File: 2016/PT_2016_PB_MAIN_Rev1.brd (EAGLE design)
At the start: 150.9 x 202.8 mm, 121 parts, among them Q1 Q_IRFS7437PbF, Q11 Q_IRFS7437PbF, Q12 2N7002, Q14 Q_IRFS7437PbF, Q16 Q_IRFS7437PbF, Q20 Q_IRFS7437PbF, Q6 Q_IRFS7437PbF, Q7 Q_IRFS7437PbF, Q9 Q_IRFS7437PbF

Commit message: Continued routing, rearranged some things
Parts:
- moved C45 45.9 mm to (125.8, 8.83), turned to 0 degrees
- moved C46 44.0 mm to (116.4, 13.8)
- moved C20 34.0 mm to (139.6, 80.7), flipped to the bottom
- moved 12V-AUX 29.2 mm to (137.9, 43.9)
- moved C43 29.2 mm to (127.3, 42.2)
- moved LED2 29.2 mm to (142.2, 34.0)
- moved R10 29.2 mm to (135.4, 34.0)
- moved U$21 29.2 mm to (128.8, 50.3)
- moved C6 29.2 mm to (127.3, 38.3)
- moved Q12 17.2 mm to (83.1, 70.1)
- moved R15 15.3 mm to (83.4, 65.3), turned to 270 degrees
- moved R8 12.5 mm to (134.6, 13.5)
- moved LED3 12.4 mm to (142.0, 13.5)
- moved 5V-AUX 12.0 mm to (138.2, 23.6)
- moved C19 11.8 mm to (119.6, 40.3), flipped to the bottom
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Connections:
- removed net 5V_AUX: U$3.P$6
- removed net N$21: U$12.DI
- removed net N$33: U$24.DI
- removed net N$43: U$4.PC4
- removed net N$48: U$4.PC5
- removed net N$65: U$4.PH2
- removed net N$91: U$4.PP0
- removed net N$92: U$4.PP1
- removed net N$93: U$4.PP2
- removed net N$97: U$4.+5V_1, U$4.+5V_2
- removed net N$99: U$4.GND_1, U$4.GND_2, U$4.GND_3, U$4.GND_4
- removed net RXD: U$12.RO
- removed net RXD1: U$24.RO
- new net RX1: U$12.RO, U$4.PC4
- new net RX2: U$24.RO, U$4.PP0
- new net TX1: U$12.DI, U$4.PC5
- new net TX2: U$24.DI, U$4.PP1
- net +5V: now also U$4.+5V_1, U$4.+5V_2
- net 12V-IMEAS: now also U$4.PH2
- net 5V-AUX: now also U$3.P$6
- net GND: now also U$4.GND_1, U$4.GND_2, U$4.GND_3, U$4.GND_4
- net PRIMARY-VMEAS: now also U$4.PP2
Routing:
- net +5V: track 228.2 -> 466.6 mm, vias 0 -> 3
- net TX2: track 0.00 -> 116.7 mm, vias 0 -> 1
- net RX2: track 0.00 -> 113.9 mm, vias 0 -> 1
- net 12V-IMEAS: track 0.00 -> 102.3 mm
- net TX1: track 0.00 -> 41.8 mm
- net RX1: track 0.00 -> 39.0 mm
- net PRIMARY-VMEAS: track 3.76 -> 34.7 mm
- net N$7: track 31.7 -> 11.8 mm
- net N$12: track 12.9 -> 0.00 mm
- net 5V-AUX: track 0.00 -> 11.8 mm
- net GND: track 153.0 -> 145.3 mm, vias 29 -> 28
- net N$4: track 56.0 -> 57.0 mm
- net N$34: track 3.70 -> 4.47 mm
- added copper zone on layer 1, net 5V-AUX
- added copper zone on layer 1, net N$7

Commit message: Continued routing.
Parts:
- moved C6 18.3 mm to (127.8, 56.6)
- moved C43 15.7 mm to (133.3, 56.6), turned to 180 degrees
- moved R10 0.76 mm to (134.6, 34.0)
- moved C46 0.60 mm to (116.4, 13.2), turned to 270 degrees
- moved C45 0.35 mm to (125.4, 8.86), turned to 270 degrees
- moved C7 0.25 mm to (16.5, 128.5), turned to 270 degrees
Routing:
- net +5V: track 466.6 -> 586.4 mm, vias 3 -> 4
- net 12V-IMEAS: track 102.3 -> 141.8 mm
- net N$9: track 0.00 -> 14.1 mm, vias 0 -> 1
- net N$12: track 0.00 -> 8.19 mm
- net 5V-AUX: track 11.8 -> 15.0 mm
- net N$15: track 0.00 -> 2.11 mm
- net N$14: track 0.00 -> 1.63 mm, vias 0 -> 1
- net GND: track 145.3 -> 144.1 mm, vias 28 -> 31
- net N$46: track 3.96 -> 4.72 mm
- added copper zone on layer 16, net 5V-AUX
- removed copper zone on layer 1, net 5V-AUX

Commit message: Routesss
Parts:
- removed U$22: TEST, MRDT-2015-General:TEST
- moved D2 14.8 mm to (76.2, 17.7)
- moved C45 7.66 mm to (118.6, 5.27), turned to 0 degrees
- moved BATT-NEG 6.86 mm to (94.5, 8.89)
- moved C46 2.98 mm to (113.5, 13.9), turned to 180 degrees
- renumbered PALPATINE-12V to POE-12V, SIDEOUS-12V to FINN-12V, U$3 to REY-5V
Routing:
- net N$7: track 11.8 -> 55.8 mm
- net PRIMARY-VMEAS: track 34.7 -> 33.4 mm
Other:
- board text added: "-"
- board text added: "REY-5V"

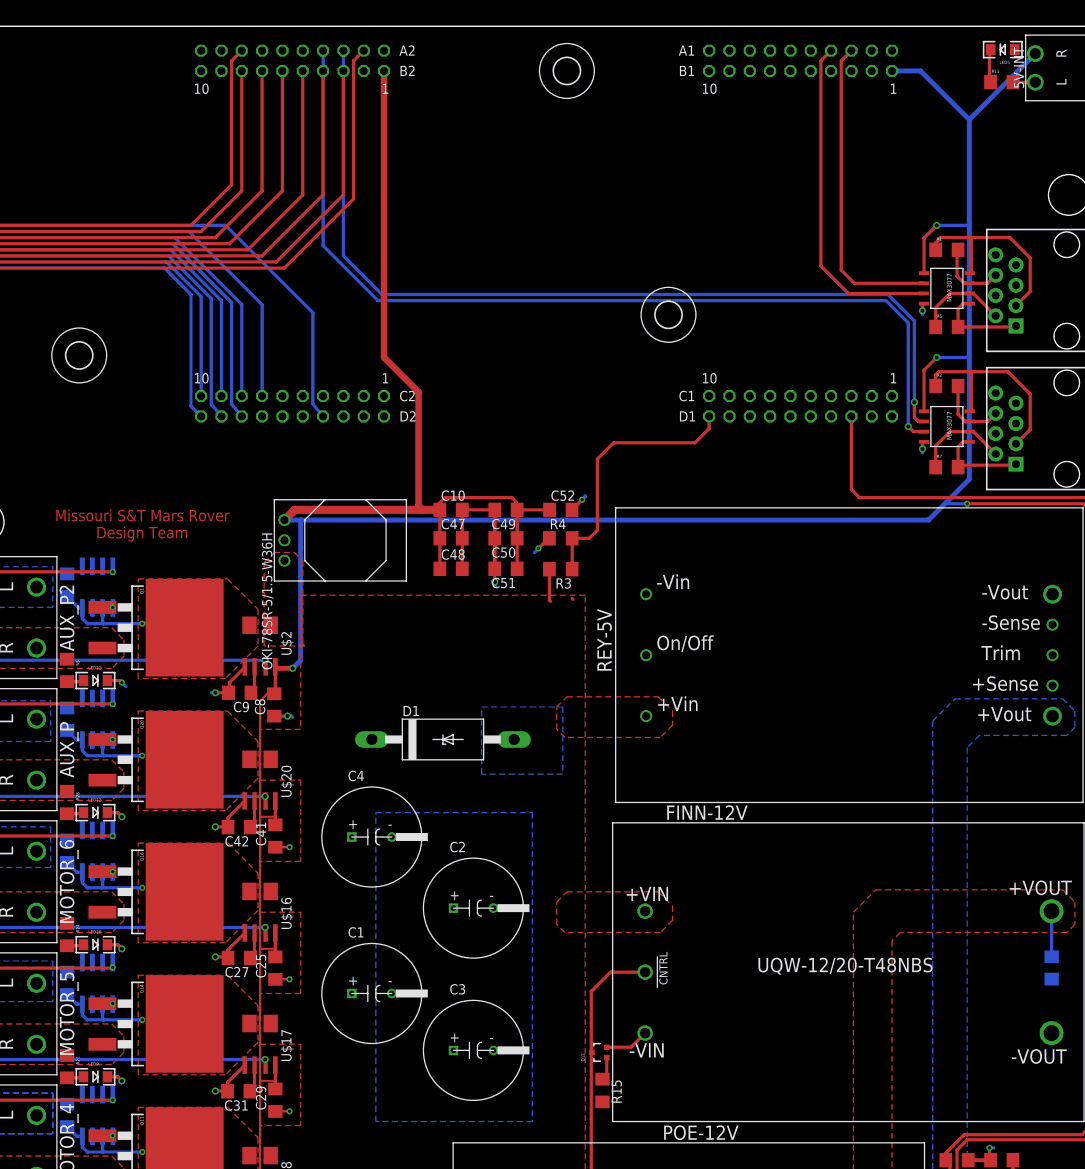
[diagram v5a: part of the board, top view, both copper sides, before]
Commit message: Minor routing changes
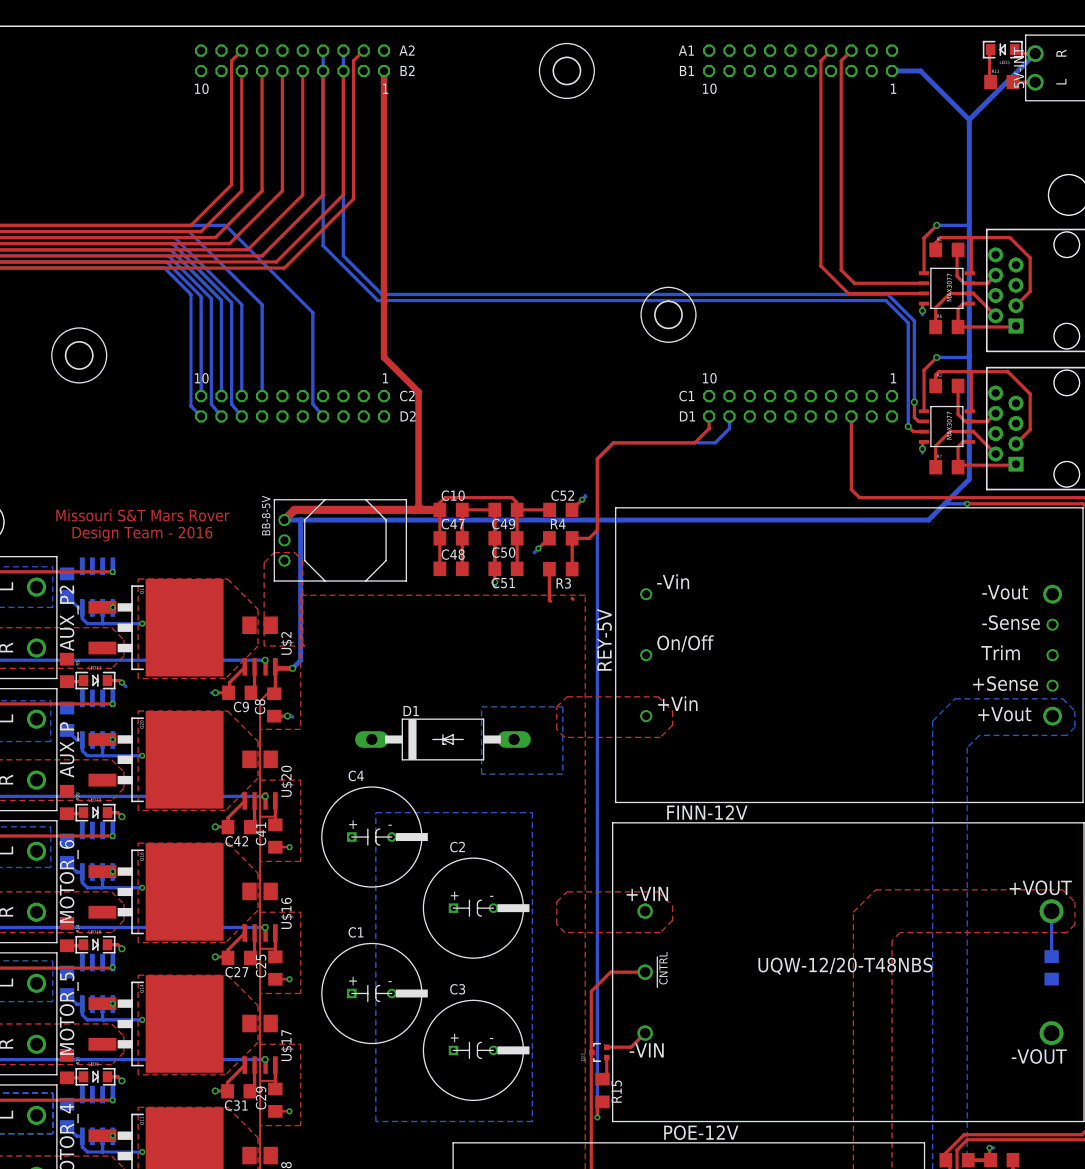
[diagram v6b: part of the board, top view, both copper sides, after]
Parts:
- renumbered OKI-78SR-5/1.5-W36H to BB-8-5V
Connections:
- removed net N$128: U$4.PN3
- net 12V-SIG: now also U$4.PN3
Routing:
- net 12V-SIG: track 0.00 -> 104.2 mm, vias 0 -> 1
- net +5V: track 586.4 -> 589.1 mm
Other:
- board text added: "Missouri S&T Mars Rover Design Team - 2016"
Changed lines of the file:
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@@
 <text x="13.462" y="-1.27" size="0.6096" layer="1" rot="R180">ROVE DOWN FOR WHAT</text>
 <text x="25.908" y="137.922" size="1.4224" layer="1" rot="R180" align="bottom-center">Missouri S&amp;T Mars Rover
-Design Team</text>
+Design Team - 2016</text>
 <text x="133.858" y="115.824" size="2.1844" layer="29" rot="R90">HORIZON / 2015</text>
 <text x="129.032" y="107.442" size="1.27" layer="29" rot="R90">Missouri S&amp;T Mars Rover Design Team</text>
@@
 <element name="C10" library="resistor" package="C1206" value="1uF" x="64.516" y="137.922"/>
 <element name="U$12" library="MAX3077" package="MAX3070E" value="MAX3077" x="126.492" y="165.608" rot="R270"/>
-<element name="OKI-78SR-5/1.5-W36H" library="MRDT-2015-PowerBoard" package="OKI-78SRH" value="Q_OKI-78SR" x="43.688" y="134.112" rot="R270"/>
+<element name="BB-8-5V" library="MRDT-2015-PowerBoard" package="OKI-78SRH" value="Q_OKI-78SR" x="43.688" y="134.112" smashed="yes" rot="R270">
+<attribute name="NAME" x="40.894" y="139.7" size="1.016" layer="25" rot="R270"/>
+</element>
 <element name="U$23" library="SparkFun-Connectors" package="RJ45-8" value="RJ45-8PTH" x="141.478" y="148.082" rot="R90"/>
 <element name="R2" library="SparkFun-Passives" package="1206" value="120 Ohm" x="126.492" y="153.416"/>
@@
 <wire x1="141.732" y1="40.132" x2="143.74" y2="38.124" width="0.4064" layer="1"/>
 <wire x1="143.74" y1="38.124" x2="143.74" y2="34.036" width="0.4064" layer="1"/>
-<contactref element="OKI-78SR-5/1.5-W36H" pad="2"/>
+<contactref element="BB-8-5V" pad="2"/>
 <wire x1="47.12" y1="-0.508" x2="47.12" y2="-2.156" width="0.4064" layer="1"/>
 <wire x1="47.12" y1="-2.156" x2="47.117" y2="-2.159" width="0.4064" layer="1"/>
@@
 <contactref element="REY-5V" pad="P$3"/>
 <wire x1="79.654" y1="126.848" x2="79.756" y2="126.746" width="0.4064" layer="1"/>
-<contactref element="OKI-78SR-5/1.5-W36H" pad="1"/>
+<contactref element="BB-8-5V" pad="1"/>
 <wire x1="76.81" y1="130.5052" x2="76.81" y2="126.644" width="0.4064" layer="1"/>
 <wire x1="76.81" y1="126.644" x2="76.962" y2="126.492" width="0.4064" layer="1"/>
@@
 <wire x1="41.656" y1="115.062" x2="42.294" y2="115.062" width="0.254" layer="1"/>
 <wire x1="42.294" y1="115.062" x2="42.418" y2="114.938" width="0.254" layer="1"/>
-<contactref element="OKI-78SR-5/1.5-W36H" pad="3"/>
+<contactref element="BB-8-5V" pad="3"/>
 <wire x1="43.688" y1="136.652" x2="44.958" y2="137.922" width="1.016" layer="1"/>
 <wire x1="44.958" y1="137.922" x2="60.96" y2="137.922" width="1.016" layer="1"/>
@@
 <via x="129.032" y="138.684" extent="1-16" drill="0.381"/>
 <wire x1="129.032" y1="138.684" x2="126.238" y2="138.684" width="0.4064" layer="16"/>
-<wire x1="137.541" y1="194.957" x2="135.128" y2="194.945" width="0" layer="19" extent="1-1"/>
+<wire x1="137.541" y1="194.957" x2="135.473" y2="194.957" width="0.4064" layer="1"/>
+<wire x1="135.473" y1="194.957" x2="134.977" y2="195.453" width="0.4064" layer="1"/>
 </signal>
 <signal name="N$4">
@@
 <signal name="12V-SIG">
 <contactref element="R15" pad="2"/>
+<contactref element="U$4" pad="PN3"/>
+<wire x1="83.439" y1="63.9195" x2="83.2235" y2="63.9195" width="0.4064" layer="1"/>
+<wire x1="83.2235" y1="63.9195" x2="82.804" y2="63.5" width="0.4064" layer="1"/>
+<wire x1="82.804" y1="63.5" x2="82.804" y2="61.976" width="0.4064" layer="1"/>
+<via x="82.804" y="61.976" extent="1-16" drill="0.381"/>
+<wire x1="82.804" y1="61.976" x2="82.804" y2="144.272" width="0.4064" layer="16"/>
+<wire x1="82.804" y1="144.272" x2="84.836" y2="146.304" width="0.4064" layer="16"/>
+<wire x1="84.836" y1="146.304" x2="97.536" y2="146.304" width="0.4064" layer="16"/>
+<wire x1="97.536" y1="146.304" x2="99.314" y2="148.082" width="0.4064" layer="16"/>
+<wire x1="99.314" y1="148.082" x2="99.314" y2="149.606" width="0.4064" layer="16"/>
 </signal>
 <signal name="N$28">
@@
 <contactref element="U$4" pad="PF3"/>
 </signal>
-<signal name="N$70">
-<contactref element="U$4" pad="PH3"/>
-</signal>
 <signal name="N$75">
 <contactref element="U$4" pad="PK4"/>
@@
 <contactref element="U$4" pad="PN2"/>
 </signal>
-<signal name="N$128">
-<contactref element="U$4" pad="PN3"/>
-</signal>
 <signal name="N$129">
 <contactref element="U$4" pad="PN4"/>
@@
 <contactref element="U$4" pad="PQ3/PA2"/>
 </signal>
+<signal name="N$21">
+<contactref element="U$4" pad="PH3"/>
+</signal>
 </signals>

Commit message: Rearranged components and routing
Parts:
- added C11: .1µF, resistor:C1206
- added C12: 1nF, resistor:C1206
- added C22: 10µF, resistor:E5-8,5
- added Q2: 2N7002, SparkFun-DiscreteSemi:SOT323
- added R11: 1k, resistor:R1206
- added U$3: ACS714LLCTR-50A-T, MRDT-2015-PowerBoard:SOIC8_ACS711
- moved C45 38.5 mm to (121.6, 43.7), turned to 270 degrees
- moved C46 38.3 mm to (116.3, 52.1), turned to 90 degrees
- moved R15 22.5 mm to (83.9, 87.8), flipped to the bottom, turned to 90 degrees
- moved C19 17.3 mm to (102.4, 39.8)
- moved POE-12V 17.3 mm to (77.0, 40.1)
- moved Q12 13.2 mm to (83.1, 83.3), flipped to the bottom, turned to 270 degrees
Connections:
- removed net N$105: U$4.PD0
- removed net N$106: U$4.PD1
- removed net N$109: U$4.PD4
- removed net N$111: U$4.PD7
- new net 5V-IMEAS: U$3.7, U$4.PD0
- new net 5V-SIG: R11.2, U$4.PN3
- new net N$38: C12.1, U$3.6
- new net N$43: Q2.3, REY-5V.P$1
- new net N$48: Q2.1, R11.1
- new net N$7: C22.+, REY-5V.P$6, REY-5V.P$7, U$3.1
- new net N$70: U$4.PH2
- new net N$89: U$4.PM6
- new net N$93: U$4.PP4
- net +5V: now also C11.2, U$3.8
- net 12V-IMEAS: now also U$4.PD1; no longer U$4.PH2
- net 12V-SIG: now also U$4.PP2; no longer U$4.PN3
- net 5V-AUX: now also U$3.4; no longer REY-5V.P$6
- net AUX_P-IMEAS: now also U$4.PB4; no longer U$4.PK7
- net AUX_P-SIG: now also U$4.PQ1; no longer U$4.PB4
- net AUX_P2-IMEAS: now also U$4.PD2; no longer U$4.PM6
- net AUX_P2-SIG: now also U$4.PK7; no longer U$4.PD2
- net GND: now also C11.1, C12.2, C22.-, Q2.2, REY-5V.P$8, U$3.5
- net M1-IMEAS: now also U$4.PK3; no longer U$4.PA7
- net M1-SIG: now also U$4.PP5; no longer U$4.PP4
- net M2-IMEAS: now also U$4.PK2; no longer U$4.PH0
- net M2-SIG: now also U$4.PA7; no longer U$4.PK3
- net M3-IMEAS: now also U$4.PK1; no longer U$4.PH1
- net M3-SIG: now also U$4.PH0; no longer U$4.PK2
- net M4-IMEAS: now also U$4.PD4; no longer U$4.PP3
- net M4-SIG: now also U$4.PH1; no longer U$4.PK1
- net M5-IMEAS: now also U$4.PK0; no longer U$4.PK6
- net M5-SIG: now also U$4.PP3; no longer U$4.PK0
- net M6-IMEAS: now also U$4.PB5; no longer U$4.PQ1
- net M6-SIG: now also U$4.PK6; no longer U$4.PB5
- net PRIMARY-VMEAS: now also U$4.PD7; no longer U$4.PP2
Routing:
- net N$33: track 55.8 -> 12.3 mm
- net +5V: track 589.1 -> 626.3 mm, vias 4 -> 7
- net TX2: track 116.7 -> 82.6 mm
- net RX2: track 113.9 -> 81.4 mm
- net 12V-SIG: track 104.2 -> 72.2 mm
- net M1-IMEAS: track 279.4 -> 250.6 mm
- net AUX_P2-SIG: track 129.2 -> 100.8 mm
- net M4-IMEAS: track 213.6 -> 188.5 mm
- net M2-IMEAS: track 251.9 -> 227.5 mm
- net M3-IMEAS: track 230.5 -> 207.2 mm
- net N$4: track 57.0 -> 79.9 mm
- net M6-IMEAS: track 174.6 -> 151.8 mm
- net M5-IMEAS: track 190.8 -> 169.8 mm
- net AUX_P2-IMEAS: track 133.7 -> 113.2 mm
- net AUX_P-SIG: track 142.7 -> 123.8 mm
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- added copper zone on layer 16, net N$7
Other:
- board size 150.9 x 202.8 mm -> 150.9 x 201.9 mm

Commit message: Mostly finished
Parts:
- added U$22: (no value), MRDT-2015-General:MRDT_LOGO
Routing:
- net 5V-IMEAS: track 0.00 -> 182.0 mm, vias 0 -> 3
- net PRIMARY-VMEAS: track 31.9 -> 83.0 mm
- net AUX_P2-IMEAS: track 113.2 -> 159.3 mm
- net AUX_P-IMEAS: track 132.1 -> 173.0 mm
- net M6-IMEAS: track 151.8 -> 189.5 mm
- net 5V-SIG: track 0.00 -> 36.0 mm, vias 0 -> 1
- net M4-IMEAS: track 188.5 -> 224.3 mm
- net TX2: track 82.6 -> 117.9 mm, vias 1 -> 2
- net M5-IMEAS: track 169.8 -> 204.4 mm
- net RX2: track 81.4 -> 114.6 mm, vias 1 -> 2
- net M3-IMEAS: track 207.2 -> 238.1 mm
- net M2-IMEAS: track 227.5 -> 253.8 mm
- net M1-IMEAS: track 250.6 -> 269.4 mm
- net 12V-IMEAS: track 132.7 -> 148.8 mm
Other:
- board text added: "Missouri S&T Mars Rover Design Team Power Board 2016"
- board text removed: "Missouri S&T Mars Rover Design Team - 2016"
